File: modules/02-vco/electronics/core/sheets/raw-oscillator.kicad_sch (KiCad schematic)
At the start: 56 parts, among them Q1 BC847BS, Q2 MMBT3906, Q3 J111, Q4 MMBFJ111, Q5 MMBT5551, U1 TL072, U2 TL072, U3 LM311

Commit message: VCO JLCPCB export done for v1.0
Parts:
- C9, Q3, R3, R6, R7, R8, R_BIAS1, R_HIFREQ1, R_WIDTH1, R_WIDTH2, TH1, TH2: CHECKED YES -> (none)
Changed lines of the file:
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@@
 			)
 		)
-		(property "CHECKED" "YES"
+		(property "CHECKED" ""
 			(at 144.78 74.93 90)
 			(effects
@@
 			)
 		)
-		(property "CHECKED" "YES"
+		(property "CHECKED" ""
 			(at 172.72 153.67 0)
 			(effects
@@
 			)
 		)
-		(property "CHECKED" "YES"
+		(property "CHECKED" ""
 			(at 102.87 62.23 90)
 			(effects
@@
 			)
 		)
-		(property "CHECKED" "YES"
+		(property "CHECKED" ""
 			(at 49.53 95.25 0)
 			(effects
@@
 			)
 		)
-		(property "CHECKED" "YES"
+		(property "CHECKED" ""
 			(at 154.94 82.55 0)
 			(effects
@@
 			)
 		)
-		(property "CHECKED" "YES"
+		(property "CHECKED" ""
 			(at 85.09 62.23 90)
 			(effects
@@
 			)
 		)
-		(property "CHECKED" "YES"
+		(property "CHECKED" ""
 			(at 222.25 59.69 90)
 			(effects
@@
 			)
 		)
-		(property "CHECKED" "YES"
+		(property "CHECKED" ""
 			(at 154.94 93.98 0)
 			(effects
@@
 			)
 		)
-		(property "CHECKED" "YES"
+		(property "CHECKED" ""
 			(at 144.78 93.98 0)
 			(effects
@@
 			)
 		)
-		(property "CHECKED" "YES"
+		(property "CHECKED" ""
 			(at 223.52 41.91 90)
 			(effects
@@
 			)
 		)
-		(property "CHECKED" "YES"
+		(property "CHECKED" ""
 			(at 123.19 74.93 90)
 			(effects
@@
 			)
 		)
-		(property "CHECKED" "YES"
+		(property "CHECKED" ""
 			(at 123.19 83.82 90)
 			(effects

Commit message: Added full BOM to VCO
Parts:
- C9, Q3, R_BIAS1, R_HIFREQ1, TH1, TH2: CHECKED (none) -> YES
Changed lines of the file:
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@@
 			)
 		)
-		(property "CHECKED" ""
+		(property "CHECKED" "YES"
 			(at 172.72 153.67 0)
 			(effects
@@
 			)
 		)
-		(property "CHECKED" ""
+		(property "CHECKED" "YES"
 			(at 49.53 95.25 0)
 			(effects
@@
 			)
 		)
-		(property "CHECKED" ""
+		(property "CHECKED" "YES"
 			(at 222.25 59.69 90)
 			(effects
@@
 			)
 		)
-		(property "CHECKED" ""
+		(property "CHECKED" "YES"
 			(at 154.94 93.98 0)
 			(effects
@@
 			)
 		)
-		(property "CHECKED" ""
+		(property "CHECKED" "YES"
 			(at 223.52 41.91 90)
 			(effects
@@
 			)
 		)
-		(property "CHECKED" ""
+		(property "CHECKED" "YES"
 			(at 123.19 83.82 90)
 			(effects

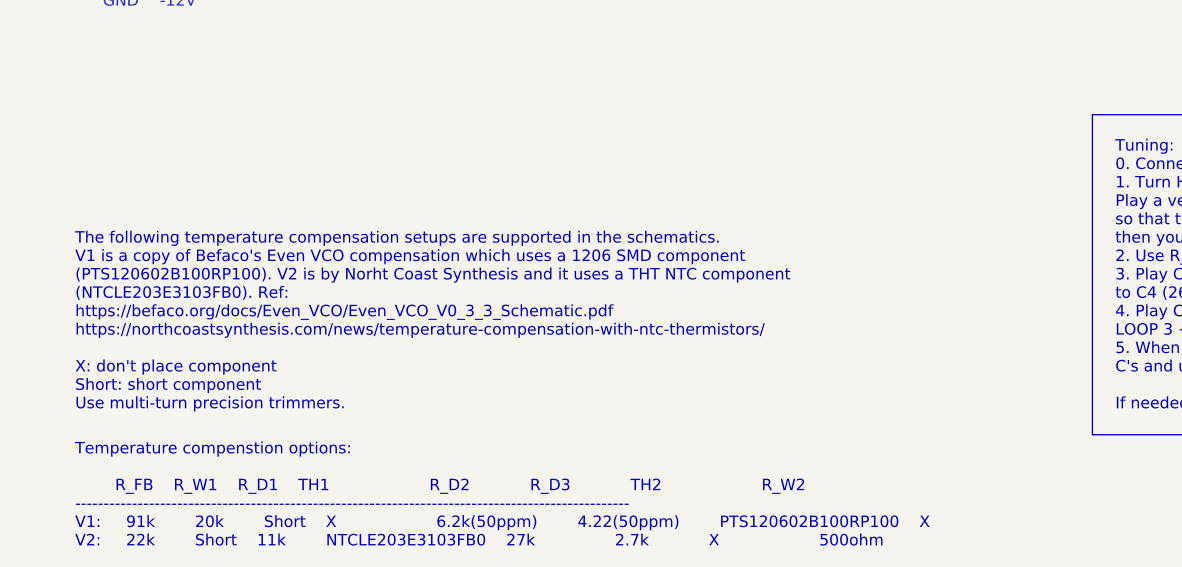
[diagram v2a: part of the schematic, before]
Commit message: Updated copy
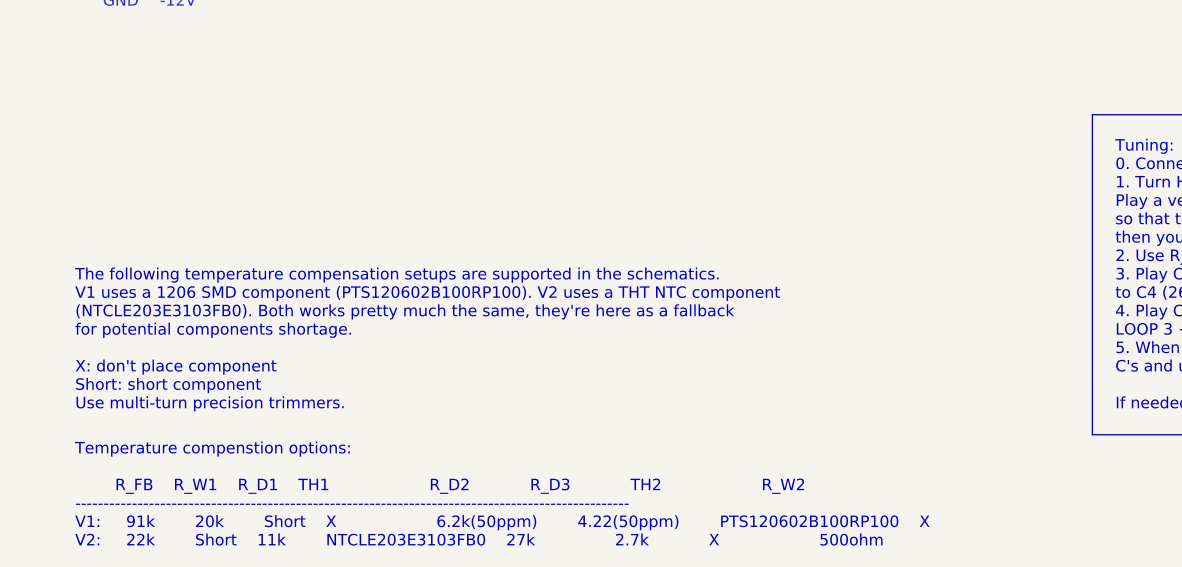
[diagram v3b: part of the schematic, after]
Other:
- note added: "The following temperature compensation setups are supported in the schematics. V1 uses a 1206 SMD component (PTS120602B100RP100). V2 uses a THT NTC component (NTCLE203E3103FB0). Both works pretty much the same, they're here as a fallback for potential components shortage. X: don't place component Short: short component Use multi-turn precision trimmers."
- note removed: "The following temperature compensation setups are supported in the schematics. V1 is a copy of Befaco's Even VCO compensation which uses a 1206 SMD component (PTS120602B100RP100). V2 is by Norht Coast Synthesis and it uses a THT NTC component (NTCLE203E3103FB0). Ref: https://befaco.org/docs/Even_VCO/Even_VCO_V0_3_3_Schematic.pdf https://northcoastsynthesis.com/news/temperature-compensation-with-n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"
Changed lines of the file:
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@@
 		)
 	)
-	(text "The following temperature compensation setups are supported in the schematics.\nV1 is a copy of Befaco's Even VCO compensation which uses a 1206 SMD component \n(PTS120602B100RP100). V2 is by Norht Coast Synthesis and it uses a THT NTC component \n(NTCLE203E3103FB0). Ref:\nhttps://befaco.org/docs/Even_VCO/Even_VCO_V0_3_3_Schematic.pdf\nhttps://northcoastsynthesis.com/news/temperature-compensation-with-ntc-thermistors/\n\nX: don't place component\nShort: short component\nUse multi-turn precision trimmers."
+	(text "The following temperature compensation setups are supported in the schematics.\nV1 uses a 1206 SMD component (PTS120602B100RP100). V2 uses a THT NTC component \n(NTCLE203E3103FB0). Both works pretty much the same, they're here as a fallback\nfor potential components shortage.\n\nX: don't place component\nShort: short component\nUse multi-turn precision trimmers."
 		(exclude_from_sim no)
 		(at 24.13 203.2 0)

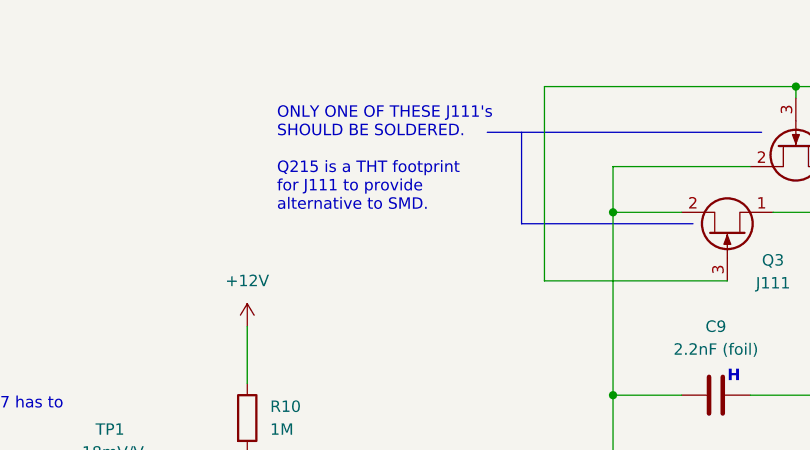
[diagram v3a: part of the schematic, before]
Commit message: Updated comment in VCO schematics
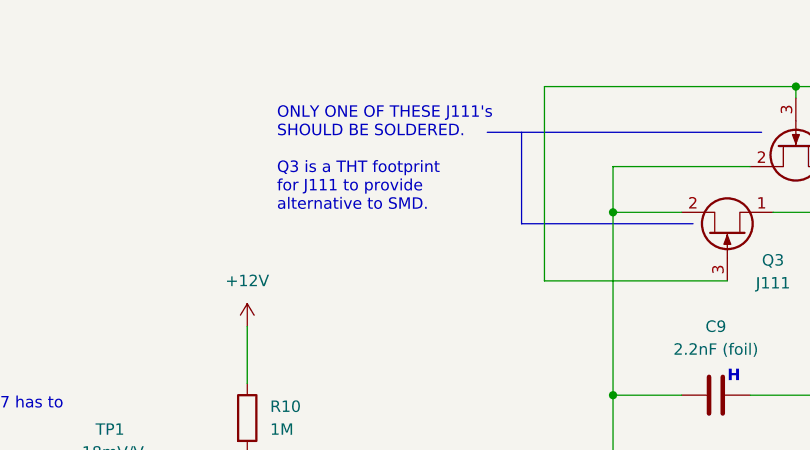
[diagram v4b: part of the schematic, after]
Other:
- note added: "ONLY ONE OF THESE J111's SHOULD BE SOLDERED. Q3 is a THT footprint for J111 to provide alternative to SMD."
- note removed: "ONLY ONE OF THESE J111's SHOULD BE SOLDERED. Q215 is a THT footprint for J111 to provide alternative to SMD."
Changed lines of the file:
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@@
 		)
 	)
-	(text "ONLY ONE OF THESE J111's\nSHOULD BE SOLDERED.\n\nQ215 is a THT footprint\nfor J111 to provide \nalternative to SMD."
+	(text "ONLY ONE OF THESE J111's\nSHOULD BE SOLDERED.\n\nQ3 is a THT footprint\nfor J111 to provide \nalternative to SMD."
 		(exclude_from_sim no)
 		(at 173.482 33.528 0)

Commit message: KiCAD version updates - PSU + VCO
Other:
- company: (none) -> Shmøergh
- title: (none) -> Moduleur VCO core
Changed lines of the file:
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@@
 	(generator_version "9.0")
 	(paper "User" 340 240)
+	(title_block
+		(title "Moduleur VCO core")
+		(date "2026-02-21")
+		(rev "v1.0")
+		(company "Shmøergh")
+	)
 	(rectangle
 		(start 137.16 170.18)

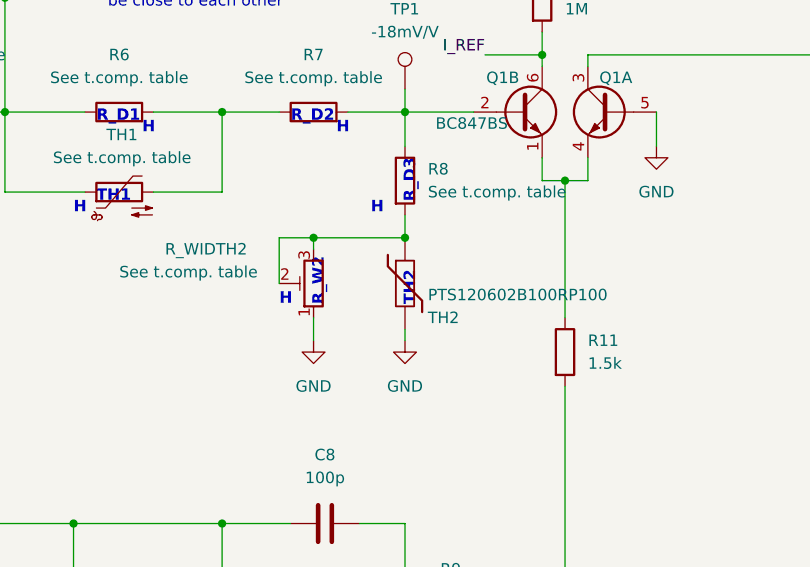
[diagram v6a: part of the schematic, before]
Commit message: Fixed VCO schemo and PCB after fckckin KiCAD update
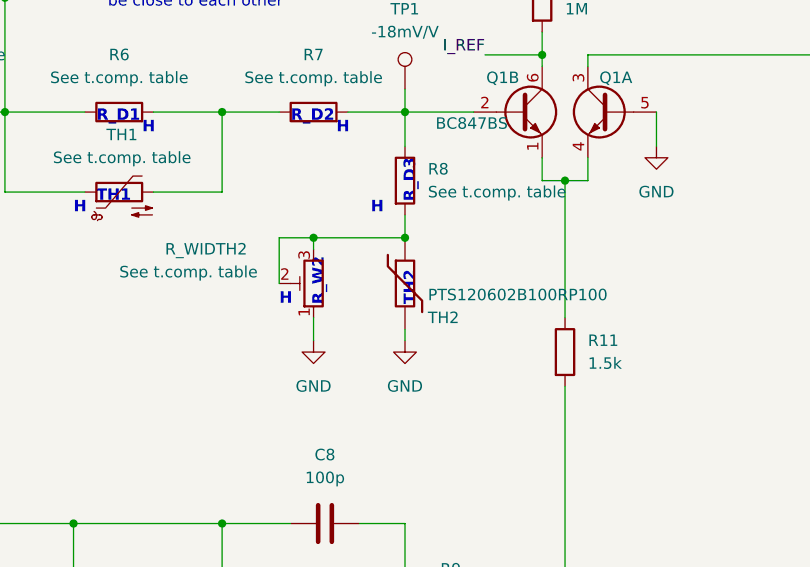
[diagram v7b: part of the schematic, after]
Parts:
- Q1: footprint Package_TO_SOT_SMD:SOT-363_SC-70-6 -> Shmoergh_Custom_Footprints:SOT-363_SC-70-6
